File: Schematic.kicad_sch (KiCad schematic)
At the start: 56 parts, among them J1 Screw_Terminal_01x04, Q1 HY1707, Q2 HY1707, Q3 S8050, Q4 2N2222, U1 UC2843A, U2 SFH618A-5, U3 TL431LP

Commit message: First working prototype - still not isolated
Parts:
- removed C1, C5: 10n, Capacitor_THT:C_Rect_L7.0mm_W2.0mm_P5.00mm, symbol Device:C
- removed C10: 1n, Capacitor_THT:C_Disc_D3.8mm_W2.6mm_P2.50mm, symbol Device:C
- removed C9: ?, Capacitor_THT:C_Rect_L7.0mm_W2.0mm_P5.00mm, symbol Device:C
- removed D2: ?, Diode_THT:D_A-405_P7.62mm_Horizontal, symbol Device:D
- removed D3: LED, LED_THT:LED_D3.0mm, symbol Device:LED
- removed Q3: S8050, Package_TO_SOT_THT:TO-92_Inline_Wide, symbol Transistor_BJT:S8050
- removed R1: 10k, Resistor_THT:R_Axial_DIN0207_L6.3mm_D2.5mm_P2.54mm_Vertical, symbol Device:R
- removed R12, R2: 1k, Resistor_THT:R_Axial_DIN0207_L6.3mm_D2.5mm_P7.62mm_Horizontal, symbol Device:R
- removed R4: 3k, Resistor_THT:R_Axial_DIN0207_L6.3mm_D2.5mm_P7.62mm_Horizontal, symbol Device:R
- removed U1: UC2843A, Package_DIP:DIP-8_W7.62mm, symbol personal:UC2843AQD8R
- added C22: 10n, Capacitor_THT:C_Disc_D3.0mm_W1.6mm_P2.50mm, symbol Device:C
- added D20: XBS104S14R-G, Diode_SMD:D_SOD-123F, symbol Device:D_Schottky
- added R20: 4.7M, Resistor_THT:R_Axial_DIN0204_L3.6mm_D1.6mm_P5.08mm_Vertical, symbol Device:R
- added R24: 4k7, Resistor_THT:R_Axial_DIN0204_L3.6mm_D1.6mm_P5.08mm_Horizontal, symbol Device:R
- added R25: 2k2, Resistor_THT:R_Axial_DIN0204_L3.6mm_D1.6mm_P2.54mm_Vertical, symbol Device:R
- added U1: UC3845, Package_DIP:DIP-8_W7.62mm, symbol personal:UC3845
- C2: value 100n -> 1n
- C20: renamed from C11; footprint Capacitor_THT:C_Disc_D7.5mm_W5.0mm_P5.00mm -> Capacitor_THT:C_Disc_D7.5mm_W5.0mm_P7.50mm
- C4: value 10n -> 1.5n
- R10, R11: value 140k -> 240k
- R2: renamed from R19; value 5k -> 10k
- R21: renamed from R15; value 15M -> 10M; footprint Resistor_THT:R_Axial_DIN0207_L6.3mm_D2.5mm_P5.08mm_Vertical -> Resistor_THT:R_Axial_DIN0204_L3.6mm_D1.6mm_P2.54mm_Vertical
- R23: renamed from R17; footprint Resistor_THT:R_Axial_DIN0204_L3.6mm_D1.6mm_P5.08mm_Horizontal -> Resistor_THT:R_Axial_DIN0204_L3.6mm_D1.6mm_P7.62mm_Horizontal
- R3: value 100k -> 5k
- R4: renamed from R20; value 1k2 -> 2k2
- R6: value 150 -> 1k
- renumbered C12 to C21, C14 to C23, C13 to C5, D1 to D21, Mod1 to Mod20, Q4 to Q20, R21 to R12, R16 to R22, R22 to R26, R18 to R27, U2 to U20, U3 to U21
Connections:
- net Comp: now also U1.1 (COMP)
- net GND: now also C22.2, U1.5 (GND)
- net Isns: now also R25.2, U1.3 (ISENSE)
- net RT_CT: now also U1.4 (RT_CT)
- net Vfb: now also U1.2 (VFB)
- net Vin+: now also U1.7 (VCC)
- net Vref: now also U1.8 (VREF)
- net at C21.2, D21.2 (A), R22.2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: now also R20.1; no longer R21.2
- net fbh: now reaches C20.1, R11.1, U21.1 (REF), VR1.3
- net at R8.1: now also D20.1 (K), R24.1, U1.6 (OUTPUT)
- new net: R20.2, R21.2
- new net Ramp: C22.1, D20.2 (A), R24.2, R25.1
- no-connect marks 23 -> 0
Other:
- moved on the sheet: C2, C20, C21, C23, C3, C4, C5, C6, C7, C8, D21, D4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

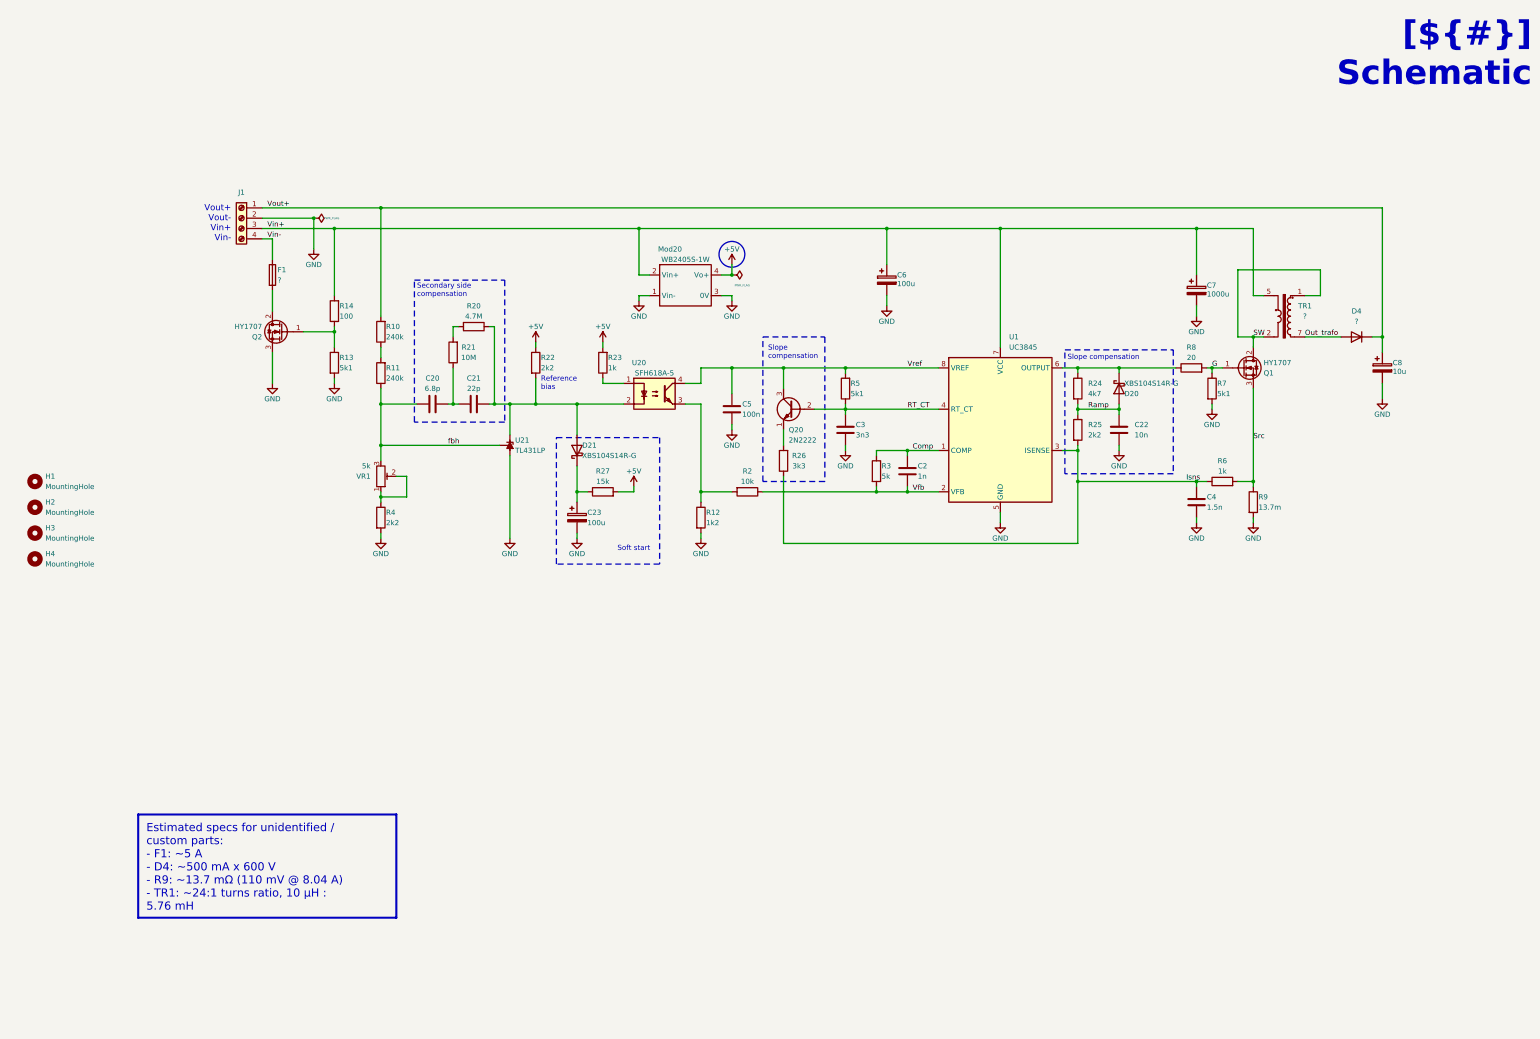
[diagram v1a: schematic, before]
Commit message: Schematic topology completed, adjusting packages
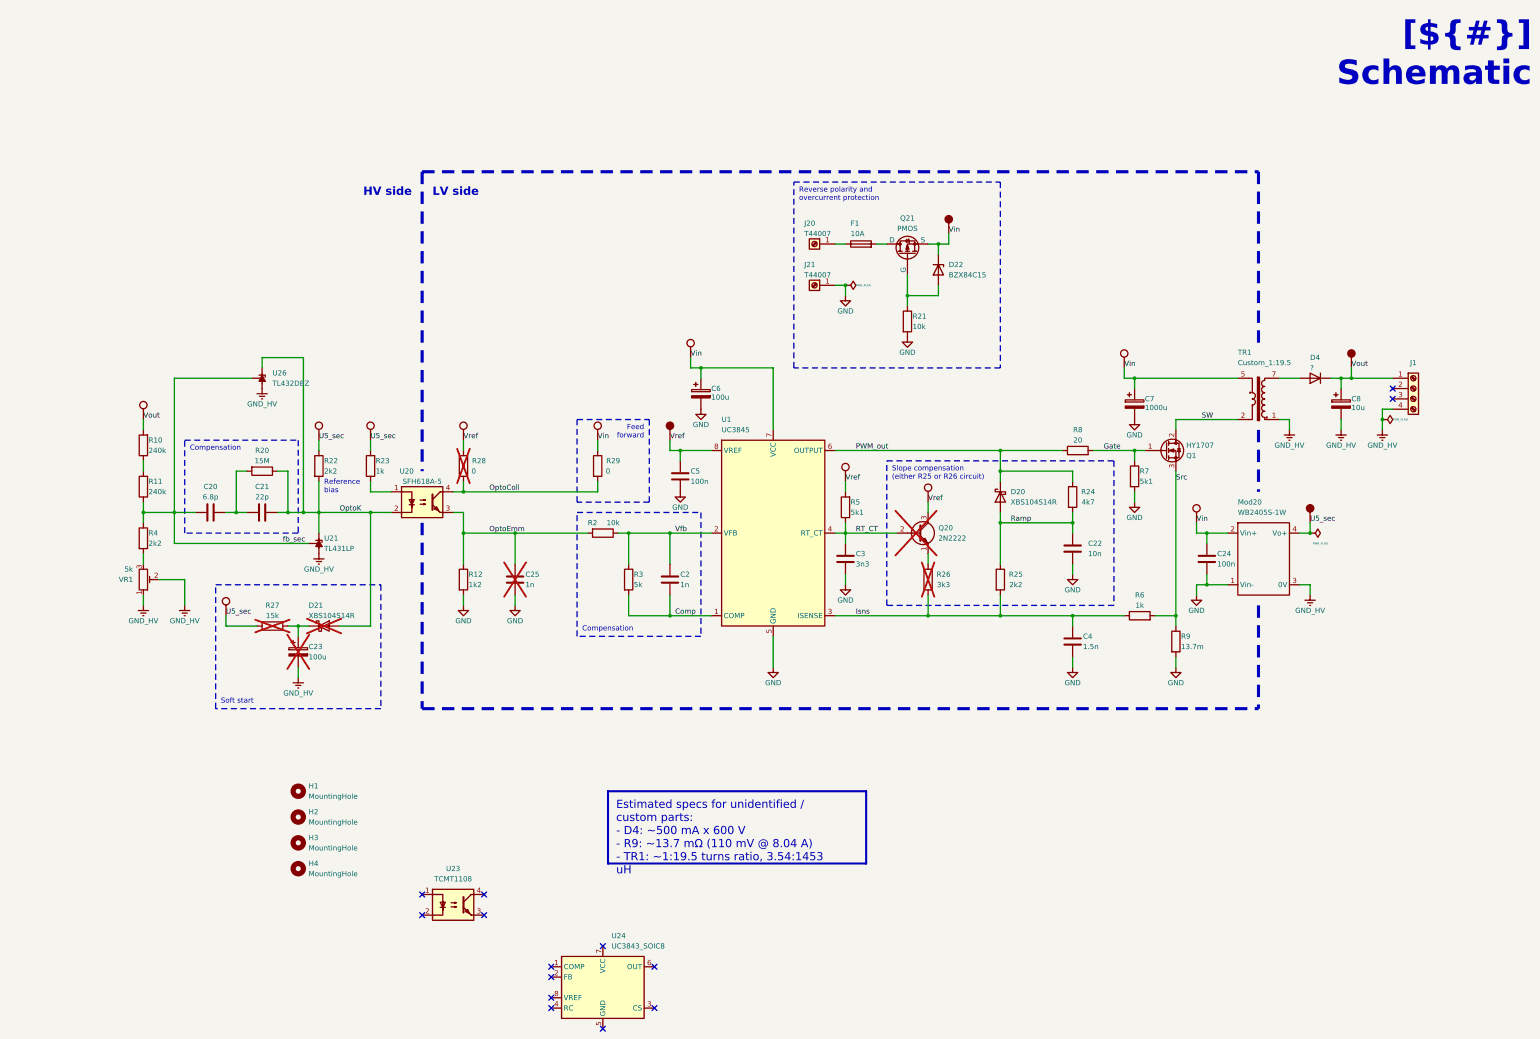
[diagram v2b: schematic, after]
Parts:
- removed Mod20: WB2405S-1W, Personal:WB___S-1W, symbol personal:WB____S-1W
- removed Q2: HY1707, Package_TO_SOT_THT:TO-220F-3_Vertical, symbol Transistor_FET:Q_NMOS_GDS
- removed R14: 100, Resistor_THT:R_Axial_DIN0207_L6.3mm_D2.5mm_P7.62mm_Horizontal, symbol Device:R
- removed R21: 10M, Resistor_THT:R_Axial_DIN0204_L3.6mm_D1.6mm_P2.54mm_Vertical, symbol Device:R
- removed TR1: ?, Personal:Tr12to450V_Alixp, symbol personal:TR_12to450V_alixp
- added C24: 100n, Capacitor_SMD:C_0603_1608Metric_Pad1.08x0.95mm_HandSolder, symbol Device:C
- added C25: 1n, Capacitor_SMD:C_0603_1608Metric_Pad1.08x0.95mm_HandSolder, symbol Device:C
- added D22: BZX84C15, Package_TO_SOT_SMD:SOT-23, symbol Diode:BZX84Cxx
- added J20, J21: T44007, Personal:T44007, symbol Connector:Screw_Terminal_01x01
- added Mod20: WB2405S-1W, Personal:WB___S-1W, symbol personal:WB____S-1W_long
- added P105, P20, P21, P22, P23, P24, P25, P30, P31, P32, P33: ~, symbol personal:Cosmetic_PWR
- added P106, P26, P28, P29: ~, symbol personal:Cosmetic_PWR_SRC
- added Q21: PMOS, symbol Simulation_SPICE:PMOS
- added R28, R29: 0, Resistor_SMD:R_0603_1608Metric_Pad0.98x0.95mm_HandSolder, symbol Device:R
- added TR1: Custom_1:19.5, Personal:Tr12to450V_Alixp, symbol personal:TR_12to450V_alixp_inv
- added U23: TCMT1108, Package_SO:SOP-4_4.4x2.6mm_P1.27mm, symbol Isolator:TCMT1108
- added U24: UC3843_SOIC8, Package_SO:SOIC-8_3.9x4.9mm_P1.27mm, symbol Regulator_Controller:UC3843_SOIC8
- added U26: TL432DBZ, Package_TO_SOT_SMD:SOT-23, symbol Reference_Voltage:TL432DBZ
- C2, C5: footprint Capacitor_THT:C_Disc_D4.3mm_W1.9mm_P5.00mm -> Capacitor_SMD:C_0603_1608Metric_Pad1.08x0.95mm_HandSolder
- C20: footprint Capacitor_THT:C_Disc_D7.5mm_W5.0mm_P7.50mm -> Capacitor_SMD:C_0603_1608Metric_Pad1.08x0.95mm_HandSolder
- C21: footprint Capacitor_THT:C_Disc_D5.0mm_W2.5mm_P5.00mm -> Capacitor_SMD:C_0603_1608Metric_Pad1.08x0.95mm_HandSolder
- C22: footprint Capacitor_THT:C_Disc_D3.0mm_W1.6mm_P2.50mm -> Capacitor_SMD:C_0603_1608Metric_Pad1.08x0.95mm_HandSolder
- C23, Q20: now not fitted
- C3: footprint Capacitor_THT:C_Rect_L4.6mm_W2.0mm_P2.50mm_MKS02_FKP02 -> Capacitor_SMD:C_0603_1608Metric_Pad1.08x0.95mm_HandSolder
- C4: footprint Capacitor_THT:C_Rect_L7.0mm_W2.0mm_P5.00mm -> Capacitor_SMD:C_0603_1608Metric_Pad1.08x0.95mm_HandSolder
- D20: value XBS104S14R-G -> XBS104S14R
- D21: value XBS104S14R-G -> XBS104S14R; now not fitted
- F1: value ? -> 10A
- R12, R22, R25: footprint Resistor_THT:R_Axial_DIN0204_L3.6mm_D1.6mm_P2.54mm_Vertical -> Resistor_SMD:R_0603_1608Metric_Pad0.98x0.95mm_HandSolder
- R2, R3, R5, R7, R8: footprint Resistor_THT:R_Axial_DIN0207_L6.3mm_D2.5mm_P7.62mm_Horizontal -> Resistor_SMD:R_0603_1608Metric_Pad0.98x0.95mm_HandSolder
- R20: value 4.7M -> 15M; footprint Resistor_THT:R_Axial_DIN0204_L3.6mm_D1.6mm_P5.08mm_Vertical -> Resistor_SMD:R_0603_1608Metric_Pad0.98x0.95mm_HandSolder
- R21: renamed from R13; value 5k1 -> 10k; footprint Resistor_THT:R_Axial_DIN0207_L6.3mm_D2.5mm_P7.62mm_Horizontal -> Resistor_SMD:R_0603_1608Metric_Pad0.98x0.95mm_HandSolder
- R23, R4: footprint Resistor_THT:R_Axial_DIN0204_L3.6mm_D1.6mm_P7.62mm_Horizontal -> Resistor_SMD:R_0603_1608Metric_Pad0.98x0.95mm_HandSolder
- R24: footprint Resistor_THT:R_Axial_DIN0204_L3.6mm_D1.6mm_P5.08mm_Horizontal -> Resistor_SMD:R_0603_1608Metric_Pad0.98x0.95mm_HandSolder
- R26: footprint Resistor_THT:R_Axial_DIN0204_L3.6mm_D1.6mm_P2.54mm_Vertical -> Resistor_SMD:R_0603_1608Metric_Pad0.98x0.95mm_HandSolder; now not fitted
- R27: footprint Resistor_THT:R_Axial_DIN0207_L6.3mm_D2.5mm_P10.16mm_Horizontal -> Resistor_SMD:R_0603_1608Metric_Pad0.98x0.95mm_HandSolder; now not fitted
- R6: footprint Resistor_THT:R_Axial_DIN0309_L9.0mm_D3.2mm_P12.70mm_Horizontal -> Resistor_SMD:R_0603_1608Metric_Pad0.98x0.95mm_HandSolder
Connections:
- net Comp: now also C2.2, R3.2; no longer C2.1, R3.1
- net GND: now also C24.2, C25.2, J21.1 (Pin_1), Mod20.1 (Vin-); no longer C23.2, C8.2, J1.2 (Pin_2), R4.2, U21.2 (A)
- net Isns: now also R26.2; no longer R26.1
- net SW: now also TR1.2
- net Vfb: now also C2.1, R3.1; no longer C2.2, R3.2
- net Vref: now also P105.1, P106.1, P20.1, P22.1, R28.1; no longer U20.4
- net OptoK: now reaches C21.2, D21.2 (A), R20.1, R22.2, U20.2, U21.3 (K)
- net OptoK: now also U26.2 (K)
- net at C20.2, C21.1: now also R20.2
- net PWM_out: now reaches D20.1 (K), R24.1, R8.1, U1.6 (OUTPUT)
- net at Q20.1 (E): now also R26.1; no longer R26.2
- net at R21.1: now also D22.1 (A), Q21.2 (G)
- net at F1.2: now also Q21.1 (D)
- net OptoEmm: now reaches R12.1, R2.2, U20.3
- net OptoEmm: now also C25.1
- net GND_HV: now reaches VR1.1, VR1.2
- net GND_HV: now also C23.2, C8.2, J1.4 (Pin_4), U21.2 (A), Mod20.3 (0V), TR1.1, U26.3 (A); no longer R4.1
- net +5V renamed U5_sec
- net U5_sec: now also Mod20.4 (Vo+), P29.1, P30.1, P31.1, P33.1
- net G renamed Gate
- net Out_trafo: no longer names the net of D4.2 (A)
- net Out_trafo: now also TR1.7
- net Vin+ renamed Vin
- net Vin: now also C24.1, D22.3 (K), Mod20.2 (Vin+), P21.1, P23.1, P24.1, P25.1, P26.1, Q21.3 (S), R29.1, TR1.5; no longer J1.3 (Pin_3)
- net Vin-: no longer names the net of F1.1
- net Vin-: now also J20.1 (Pin_1); no longer J1.4 (Pin_4)
- net Vout+ renamed Vout
- net Vout: now also P28.1, P32.1
- net fbh renamed fb_sec
- net fb_sec: now also R4.1, U26.1 (REF); no longer VR1.3
- new net: R4.2, VR1.3
- new net OptoColl: R28.2, R29.2, U20.4
- no-connect marks 0 -> 14
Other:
- note added: "Compensation"
- note added: "Feed forward"
- note added: "HV side"
- note added: "LV side"
- note added: "Reverse polarity and overcurrent protection"
- note added: "Slope compensation (either R25 or R26 circuit)"
- note removed: "Secondary side compensation"
- note removed: "Slope compensation"
- note removed: "Vout+ Vout- Vin+ Vin-"
- moved on the sheet: C2, C20, C21, C22, C3, C4, C5, C6, C7, C8, D20, D4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

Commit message: Several footprint updates
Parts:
- removed C6: 100u, Capacitor_THT:C_Radial_D8.0mm_H11.5mm_P3.50mm, symbol Device:C_Polarized
- removed Q20: 2N2222, Package_TO_SOT_THT:TO-92L_Inline_Wide, symbol Transistor_BJT:2N3904
- removed U20: SFH618A-5, Package_DIP:DIP-4_W7.62mm, symbol Isolator:SFH617A-1
- removed U21: TL431LP, Package_TO_SOT_THT:TO-92L_Inline_Wide, symbol Reference_Voltage:TL431LP
- removed U24: UC3843_SOIC8, Package_SO:SOIC-8_3.9x4.9mm_P1.27mm, symbol Regulator_Controller:UC3843_SOIC8
- added C26: 100n, Capacitor_SMD:C_0603_1608Metric_Pad1.08x0.95mm_HandSolder, symbol Device:C
- added C6: 4.7u, Capacitor_SMD:C_0805_2012Metric_Pad1.18x1.45mm_HandSolder, symbol Device:C
- added D23: BZT52B5V1, Diode_SMD:D_SOD-123, symbol Device:D_Zener
- added Q20: BC817, Package_TO_SOT_SMD:SOT-23, symbol Transistor_BJT:BC817
- D20: value XBS104S14R -> PMEG4010CEH; symbol Device:D_Schottky -> Diode:PMEG4010CEH
- D21: value XBS104S14R -> 1N4148W; footprint Diode_SMD:D_SOD-123F -> Diode_SMD:D_SOD-123; symbol Device:D_Schottky -> Diode:1N4148W
- D22: value BZX84C15 -> BZT52B15; footprint Package_TO_SOT_SMD:SOT-23 -> Diode_SMD:D_SOD-123; symbol Diode:BZX84Cxx -> Diode:BZT52Bxx
- F1: footprint Fuse:Fuseholder_Clip-5x20mm_Eaton_1A5601-01_Inline_P20.80x6.76mm_D1.70mm_Horizontal -> Fuse:Fuseholder_Clip-5x20mm_Littelfuse_520_Inline_P20.50x5.80mm_D1.30mm_Horizontal
- R26: value 3k3 -> 1k; now fitted
- U1: footprint Package_DIP:DIP-8_W7.62mm -> Package_SO:JEITA_SOIC-8_3.9x4.9mm_P1.27mm
- U21: renamed from U26; value TL432DBZ -> TL431M; Link (none) -> https://www.lcsc.com/product-detail/C48947167.html; MPN (none) -> FOSAN TL431M-0.3%-6AF
- renumbered U23 to U20
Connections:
- net OptoColl is gone; now on net OpCol: R28.2, R29.2
- net OptoEmm is gone; now on net OpEm: C25.1, R12.1, R2.2
- net OptoK is gone; now on net OpK: C21.2, D21.2 (A), R20.1, R22.2, U21.2 (K)
- net GND: now also C26.2, C6.2, D23.2 (A)
- net Isns: no longer R25.2
- net Ramp: now also R26.1; no longer R24.2
- net Vin: now also D22.1 (K), C26.1, C6.1; no longer D22.3 (K)
- net Vref: now also Q20.3 (C)
- net at Q21.2 (G), R21.1: now also D22.2 (A); no longer D22.1 (A)
- net OpA: now reaches U20.1
- net OpA: now also R23.1
- net OpK: now reaches U20.2
- net OpEm: now reaches U20.3
- net OpEm: now also D23.1 (K)
- net OpCol: now reaches U20.4
- net fb_sec renamed Ref_sns
- new net: Q20.1 (B), R24.2
- new net: Q20.2 (E), R25.2
- no-connect marks 14 -> 2
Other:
- note added: "Slope compensation"
- note removed: "Slope compensation (either R25 or R26 circuit)"
- moved on the sheet: C2, C20, C21, C22, C23, C24, C25, C3, C4, C5, C7, C8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

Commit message: Layout started
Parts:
- added Q22: IRF4905, Package_TO_SOT_THT:TO-220-3_Vertical, symbol Transistor_FET:IRF4905
- D4: value ? -> UF4007
- Q21: value PMOS -> SUD50P06-15; footprint (none) -> Package_TO_SOT_SMD:TO-252-2; symbol Simulation_SPICE:PMOS -> Transistor_FET:SUD50P06-15
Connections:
- net Vin: now also F1.1, J20.1 (Pin_1); no longer C24.1, C26.1, C6.1, C7.1, D22.1 (K), Mod20.2 (Vin+), P21.1, P23.1, P24.1, P25.1, P26.1, Q21.3 (S), R29.1, TR1.5, U1.7 (VCC)
- net SS_cap: now reaches C23.1, D21.1 (K), R27.1
- net RP_Gate: now reaches D22.2 (A), R21.1
- net RP_Gate: now also Q22.1 (G); no longer Q21.2 (G)
- net TR_out: now reaches D4.2 (A), TR1.7
- net at Q21.1 (G): no longer F1.2
- new net Vin_f: F1.2, Q22.2 (D)
- new net Vin_p: C24.1, C26.1, C6.1, C7.1, D22.1 (K), Mod20.2 (Vin+), P21.1, P23.1, P24.1, P25.1, P26.1, Q22.3 (S), R29.1, TR1.5, U1.7 (VCC)
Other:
- moved on the sheet: C8, D22, D4, F1, J1, J20, J21, Q21, R21, R27

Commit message: Layout candidate drafted
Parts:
- removed Q22: IRF4905, Package_TO_SOT_THT:TO-220-3_Vertical, symbol Transistor_FET:IRF4905
- U1: footprint Package_SO:JEITA_SOIC-8_3.9x4.9mm_P1.27mm -> Package_DIP:DIP-8_W7.62mm
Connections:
- net RP_Gate: now also Q21.1 (G)
- net Vin_f: now also Q21.2 (D)
- net Vin_p: now also Q21.3 (S)
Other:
- moved on the sheet: Q21
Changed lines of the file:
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@@
 			)
 		)
-		(property "Footprint" "Package_SO:JEITA_SOIC-8_3.9x4.9mm_P1.27mm"
+		(property "Footprint" "Package_DIP:DIP-8_W7.62mm"
 			(at 236.22 158.75 0)
 			(effects
@@
 	)
 	(symbol
-		(lib_id "Transistor_FET:IRF4905")
-		(at 264.16 71.12 90)
-		(unit 1)
-		(exclude_from_sim no)
-		(in_bom yes)
-		(on_board yes)
-		(dnp no)
-		(fields_autoplaced yes)
-		(property "Reference" "Q22"
-			(at 264.16 62.23 90)
-			(effects
-				(font
-					(size 1.27 1.27)
-				)
-			)
-		)
-		(property "Value" "IRF4905"
-			(at 264.16 64.77 90)
-			(effects
-				(font
-					(size 1.27 1.27)
-				)
-			)
-		)
-		(property "Footprint" "Package_TO_SOT_THT:TO-220-3_Vertical"
-			(at 266.065 66.04 0)
-			(effects
-				(font
-					(size 1.27 1.27)
-					(italic yes)
-				)
-				(justify left)
-				(hide yes)
-			)
-		)
-		(property "Datasheet" "http://www.infineon.com/dgdl/irf4905.pdf?fileId=5546d462533600a4015355e32165197c"
-			(at 267.97 66.04 0)
-			(effects
-				(font
-					(size 1.27 1.27)
-				)
-				(justify left)
-				(hide yes)
-			)
-		)
-		(property "Description" "-74A Id, -55V Vds, Single P-Channel HEXFET Power MOSFET, 20mOhm Ron, TO-220AB"
-			(at 264.16 71.12 0)
-			(effects
-				(font
-					(size 1.27 1.27)
-				)
-				(hide yes)
-			)
-		)
-		(pin "2"
-		)
-		(pin "1"
-		)
-		(pin "3"
-		)
-		(instances
-			(project ""
-				(path "/f9e05184-c88b-4a88-ae9c-ab2bdb32be7c/82da9dbf-ba38-4d08-ba35-a220fa2963b1/b0fdce11-0fa7-4399-9147-4b60eb490e1b"
-					(reference "Q22")
-					(unit 1)
-				)
-			)
-		)
-	)
-	(symbol
 		(lib_id "Device:R")
 		(at 60.96 140.97 0)
@@
 	(symbol
 		(lib_id "Transistor_FET:SUD50P06-15")
-		(at 210.82 67.31 90)
+		(at 264.16 71.12 90)
 		(unit 1)
 		(exclude_from_sim no)
@@
 		(fields_autoplaced yes)
 		(property "Reference" "Q21"
-			(at 210.82 58.42 90)
+			(at 264.16 62.23 90)
 			(effects
 				(font
@@
 		)
 		(property "Value" "SUD50P06-15"
-			(at 210.82 60.96 90)
+			(at 264.16 64.77 90)
 			(effects
 				(font
@@
 		)
 		(property "Footprint" "Package_TO_SOT_SMD:TO-252-2"
-			(at 212.725 62.357 0)
+			(at 266.065 66.167 0)
 			(effects
 				(font
@@
 		)
 		(property "Datasheet" "https://www.vishay.com/docs/68940/sud50p06.pdf"
-			(at 214.63 62.23 0)
+			(at 267.97 66.04 0)
 			(effects
 				(font
@@
 		)
 		(property "Description" "-50A Id, -60V Vds, TrenchFET P-Channel Power MOSFET, 15mOhm Ron, 165nC Qg, -55 to 150 °C, TO-252-2"
-			(at 210.82 67.31 0)
+			(at 264.16 71.12 0)
 			(effects
 				(font

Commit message: Layout candidate #2 (draft)
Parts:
- added C27: 4.7u, Capacitor_SMD:C_0805_2012Metric_Pad1.18x1.45mm_HandSolder, symbol Device:C
- added C28: 100u, Capacitor_THT:CP_Radial_D6.3mm_P2.50mm, symbol Device:C_Polarized
- C23: footprint Capacitor_THT:CP_Radial_D8.0mm_P2.50mm -> Capacitor_THT:CP_Radial_D6.3mm_P2.50mm
- C24: value 100n -> 4.7u; footprint Capacitor_SMD:C_0603_1608Metric_Pad1.08x0.95mm_HandSolder -> Capacitor_SMD:C_0805_2012Metric_Pad1.18x1.45mm_HandSolder
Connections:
- net GND: now also C27.2
- net GND_HV: now also C28.2
- net U5_sec: now also C28.1
- net Vin_p: now also C27.1
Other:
- moved on the sheet: C2, C20, C21, C22, C23, C25, C26, C3, C4, C5, C6, C7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
